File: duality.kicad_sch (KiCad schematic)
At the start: 0 parts

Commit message: develop: Started adding more stuff. Started symbol for FPGA.
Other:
- added sheet FPGA (fpga.kicad_sch)
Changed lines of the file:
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@@
+		)
+	)
+	(sheet
+		(at 107.95 52.07)
+		(size 21.59 13.97)
+		(exclude_from_sim no)
+		(in_bom yes)
+		(on_board yes)
+		(dnp no)
+		(fields_autoplaced yes)
+		(stroke
+			(width 0.1524)
+			(type solid)
+		)
+		(fill
+			(color 0 0 0 0.0000)
+		)
+		(property "Sheetname" "FPGA"
+			(at 107.95 51.3584 0)
+			(effects
+				(font
+					(size 1.27 1.27)
+				)
+				(justify left bottom)
+			)
+		)
+		(property "Sheetfile" "fpga.kicad_sch"
+			(at 107.95 66.6246 0)
+			(effects
+				(font
+					(size 1.27 1.27)
+				)
+				(justify left top)
+			)
+		)
+		(instances
+			(project "duality"
+				(path "/ba4aeeea-982a-4252-9638-c2cfeb24b844"
+					(page "5")
+				)
+			)
 		)
 	)

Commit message: develop: Did some stuff. Not sure what I am doing :).
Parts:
- added J1, J3, J4: USB_C_Receptacle_USB2.0_14P, symbol Connector:USB_C_Receptacle_USB2.0_14P
- added J2, J5: RJ45_RB1-125B8G1A, Connector_RJ:RJ45_UDE_RB1-125B8G1A, symbol Connector:RJ45_RB1-125B8G1A
- added R2, R3: 5.1k, symbol Device:R
- added U5: USB3740B-AI2, symbol Interface_USB:USB3740B-AI2
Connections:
- new net: J3.A4 (VBUS), J3.A9 (VBUS), J3.B4 (VBUS), J3.B9 (VBUS)
- new net: J3.A5 (CC1), R3.1
- new net: J3.B5 (CC2), R2.1
- new net: J4.A1 (GND), J4.A12 (GND), J4.B1 (GND), J4.B12 (GND)
- new net: J4.A4 (VBUS), J4.A9 (VBUS), J4.B4 (VBUS), J4.B9 (VBUS)
- new net: J1.A1 (GND), J1.A12 (GND), J1.B1 (GND), J1.B12 (GND)
- new net: J1.A4 (VBUS), J1.A9 (VBUS), J1.B4 (VBUS), J1.B9 (VBUS)
- new net GND: J3.A1 (GND), J3.A12 (GND), J3.B1 (GND), J3.B12 (GND), R2.2, R3.2

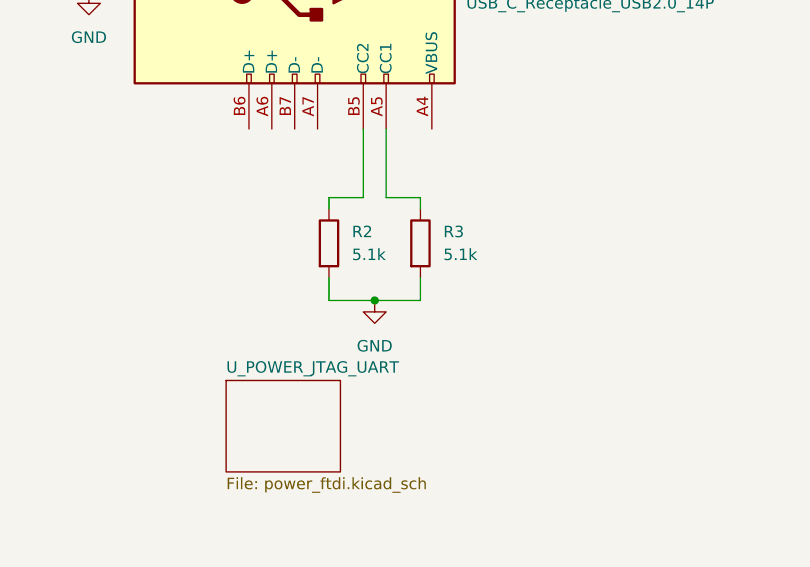
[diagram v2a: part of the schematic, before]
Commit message: develop: Added 1.8/3.3V and 0.95V power regulators.
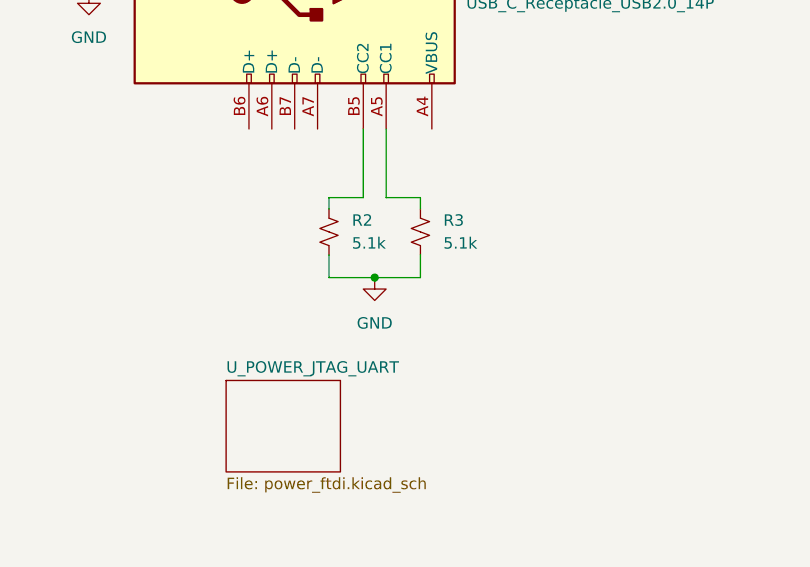
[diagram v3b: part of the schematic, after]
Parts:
- R2, R3: symbol Device:R -> Device:R_Small_US
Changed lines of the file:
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@@
 	(paper "A4")
 	(junction
-		(at 158.75 63.5)
+		(at 158.75 60.96)
 		(diameter 0)
 		(color 0 0 0 0)
@@
 	(wire
 		(pts
-			(xy 153.67 60.96) (xy 153.67 63.5)
+			(xy 153.67 58.42) (xy 153.67 60.96)
 		)
 		(stroke
@@
 	(wire
 		(pts
-			(xy 163.83 60.96) (xy 163.83 63.5)
-		)
-		(stroke
-			(width 0)
-			(type default)
-		)
-	)
-	(wire
-		(pts
-			(xy 153.67 63.5) (xy 158.75 63.5)
+			(xy 163.83 58.42) (xy 163.83 60.96)
+		)
+		(stroke
+			(width 0)
+			(type default)
+		)
+	)
+	(wire
+		(pts
+			(xy 153.67 60.96) (xy 158.75 60.96)
 		)
 		(stroke
@@
 	(wire
 		(pts
-			(xy 158.75 63.5) (xy 163.83 63.5)
+			(xy 158.75 60.96) (xy 163.83 60.96)
 		)
 		(stroke
@@
 	)
 	(symbol
-		(lib_id "Device:R")
-		(at 163.83 57.15 0)
+		(lib_id "Device:R_Small_US")
+		(at 163.83 55.88 0)
 		(unit 1)
 		(exclude_from_sim no)
@@
 		(fields_autoplaced yes)
 		(property "Reference" "R3"
-			(at 166.37 55.8799 0)
+			(at 166.37 54.6099 0)
 			(effects
 				(font
@@
 		)
 		(property "Value" "5.1k"
-			(at 166.37 58.4199 0)
+			(at 166.37 57.1499 0)
 			(effects
 				(font
@@
 		)
 		(property "Footprint" ""
-			(at 162.052 57.15 90)
+			(at 163.83 55.88 0)
 			(effects
 				(font
@@
 		)
 		(property "Datasheet" "~"
-			(at 163.83 57.15 0)
-			(effects
-				(font
-					(size 1.27 1.27)
-				)
-				(hide yes)
-			)
-		)
-		(property "Description" "Resistor"
-			(at 163.83 57.15 0)
+			(at 163.83 55.88 0)
+			(effects
+				(font
+					(size 1.27 1.27)
+				)
+				(hide yes)
+			)
+		)
+		(property "Description" "Resistor, small US symbol"
+			(at 163.83 55.88 0)
 			(effects
 				(font
@@
 	(symbol
 		(lib_id "power:GND")
-		(at 158.75 63.5 0)
+		(at 158.75 60.96 0)
 		(unit 1)
 		(exclude_from_sim no)
@@
 		(fields_autoplaced yes)
 		(property "Reference" "#PWR02"
-			(at 158.75 69.85 0)
+			(at 158.75 67.31 0)
 			(effects
 				(font
@@
 		)
 		(property "Value" "GND"
-			(at 158.75 68.58 0)
+			(at 158.75 66.04 0)
 			(effects
 				(font
@@
 		)
 		(property "Footprint" ""
-			(at 158.75 63.5 0)
+			(at 158.75 60.96 0)
 			(effects
 				(font
@@
 		)
 		(property "Datasheet" ""
-			(at 158.75 63.5 0)
+			(at 158.75 60.96 0)
 			(effects
 				(font
@@
 		)
 		(property "Description" "Power symbol creates a global label with name \"GND\" , ground"
-			(at 158.75 63.5 0)
+			(at 158.75 60.96 0)
 			(effects
 				(font
@@
 	)
 	(symbol
-		(lib_id "Device:R")
-		(at 153.67 57.15 0)
+		(lib_id "Device:R_Small_US")
+		(at 153.67 55.88 0)
 		(unit 1)
 		(exclude_from_sim no)
@@
 		(fields_autoplaced yes)
 		(property "Reference" "R2"
-			(at 156.21 55.8799 0)
+			(at 156.21 54.6099 0)
 			(effects
 				(font
@@
 		)
 		(property "Value" "5.1k"
-			(at 156.21 58.4199 0)
+			(at 156.21 57.1499 0)
 			(effects
 				(font
@@
 		)
 		(property "Footprint" ""
-			(at 151.892 57.15 90)
+			(at 153.67 55.88 0)
 			(effects
 				(font
@@
 		)
 		(property "Datasheet" "~"
-			(at 153.67 57.15 0)
-			(effects
-				(font
-					(size 1.27 1.27)
-				)
-				(hide yes)
-			)
-		)
-		(property "Description" "Resistor"
-			(at 153.67 57.15 0)
-			(effects
-				(font
+			(at 153.67 55.88 0)
+			(effects
+				(font
+					(size 1.27 1.27)
+				)
+				(hide yes)
+			)
+		)
+		(property "Description" "Resistor, small US symbol"
+			(at 153.67 55.88 0)
+			(effects
+				(font
